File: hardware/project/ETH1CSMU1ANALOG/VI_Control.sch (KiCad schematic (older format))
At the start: 156 parts

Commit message: Base board schematic.
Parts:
- added C? (x2): 2u2, symbol Device:C
- added C? (x2): 100n, symbol Device:C
- added D? (x2): BZT52B15LP, symbol Device:D_Zener
- added R? (x2): 2k2, symbol Device:R
- added R? (x2): 3k57, symbol Device:R
- added U?: ADS8517, symbol ETH1CSMU1:ADS8517
- TP?: value +/- -> POLARITY
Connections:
- net +15VF: now also U?.13 (V+), U?.13 (V+), U?.13 (V+), U?.6 (V+), U?.6 (V+), U?.6 (V+), R?.2
- net -15VF: now also U?.2 (V-), U?.2 (V-), U?.2 (V-), U?.4 (V-), U?.4 (V-), U?.4 (V-), R?.2
- net GNDB: now also C?.2, C?.2
- net GNDP: now also C?.2, C?.2, U?.14 (DGND), U?.2 (AGND1), U?.20 (TAG), U?.25 (PWRD), U?.26 (REFD), U?.6 (AGND2), U?.7 (SB/~BTC)
- net GNDS: now also U?.21 (BYTE)
- net at C?.2, R?.2, U?.6: now also U?.1 (R1IN)
- net +3.3VF renamed +3.3DVF
- net +3.3DVF: now also U?.28 (VDIG), U?.8 (EXT/~IN)
- new net: C?.1, U?.3 (R2IN), U?.4 (CAP)
- new net: C?.1, U?.5 (REF)
- new net +30VF: C?.1, R?.2
- new net +5VF: U?.27 (VANA)
- new net +BOT_DRIVE: D?.2 (A)
- new net +TOP_DRIVE: D?.1 (K), R?.1
- new net +ZENER: R?.1
- new net -30VF: C?.1, R?.2
- new net -BOT_DRIVE: D?.1 (K)
- new net -TOP_DRIVE: D?.2 (A), R?.1
- new net -ZENER: R?.1
- new net ADC_DATACLK: U?.18 (DATACLK)
- new net ADC_R\~C: U?.22 (R/~C)
- new net ADC_SDATA: U?.19 (SDATA)
- new net ADC_~BUSY: U?.24 (~BUSY)
- new net ADC_~CS: U?.23 (~CS)
- no-connect marks 18 -> 26
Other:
- moved on the sheet: TP?

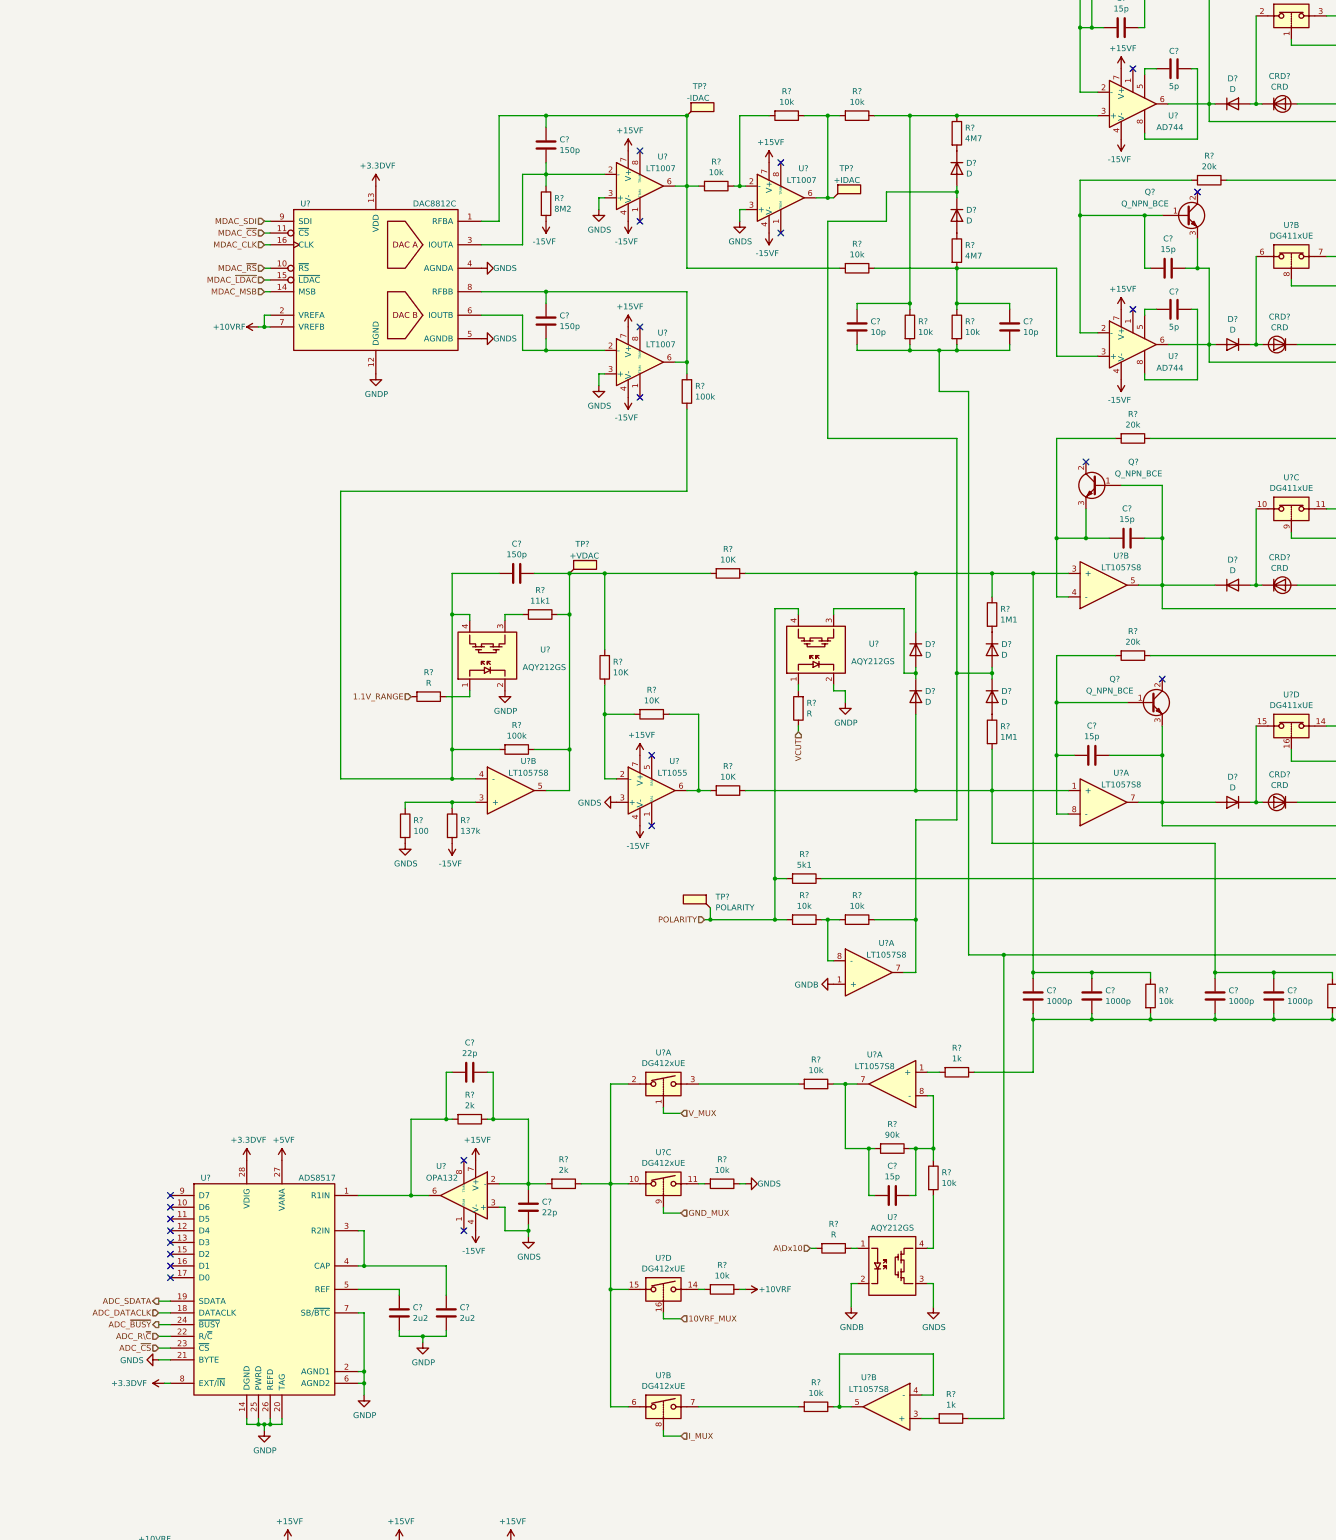
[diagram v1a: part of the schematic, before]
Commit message: Footprint assigment
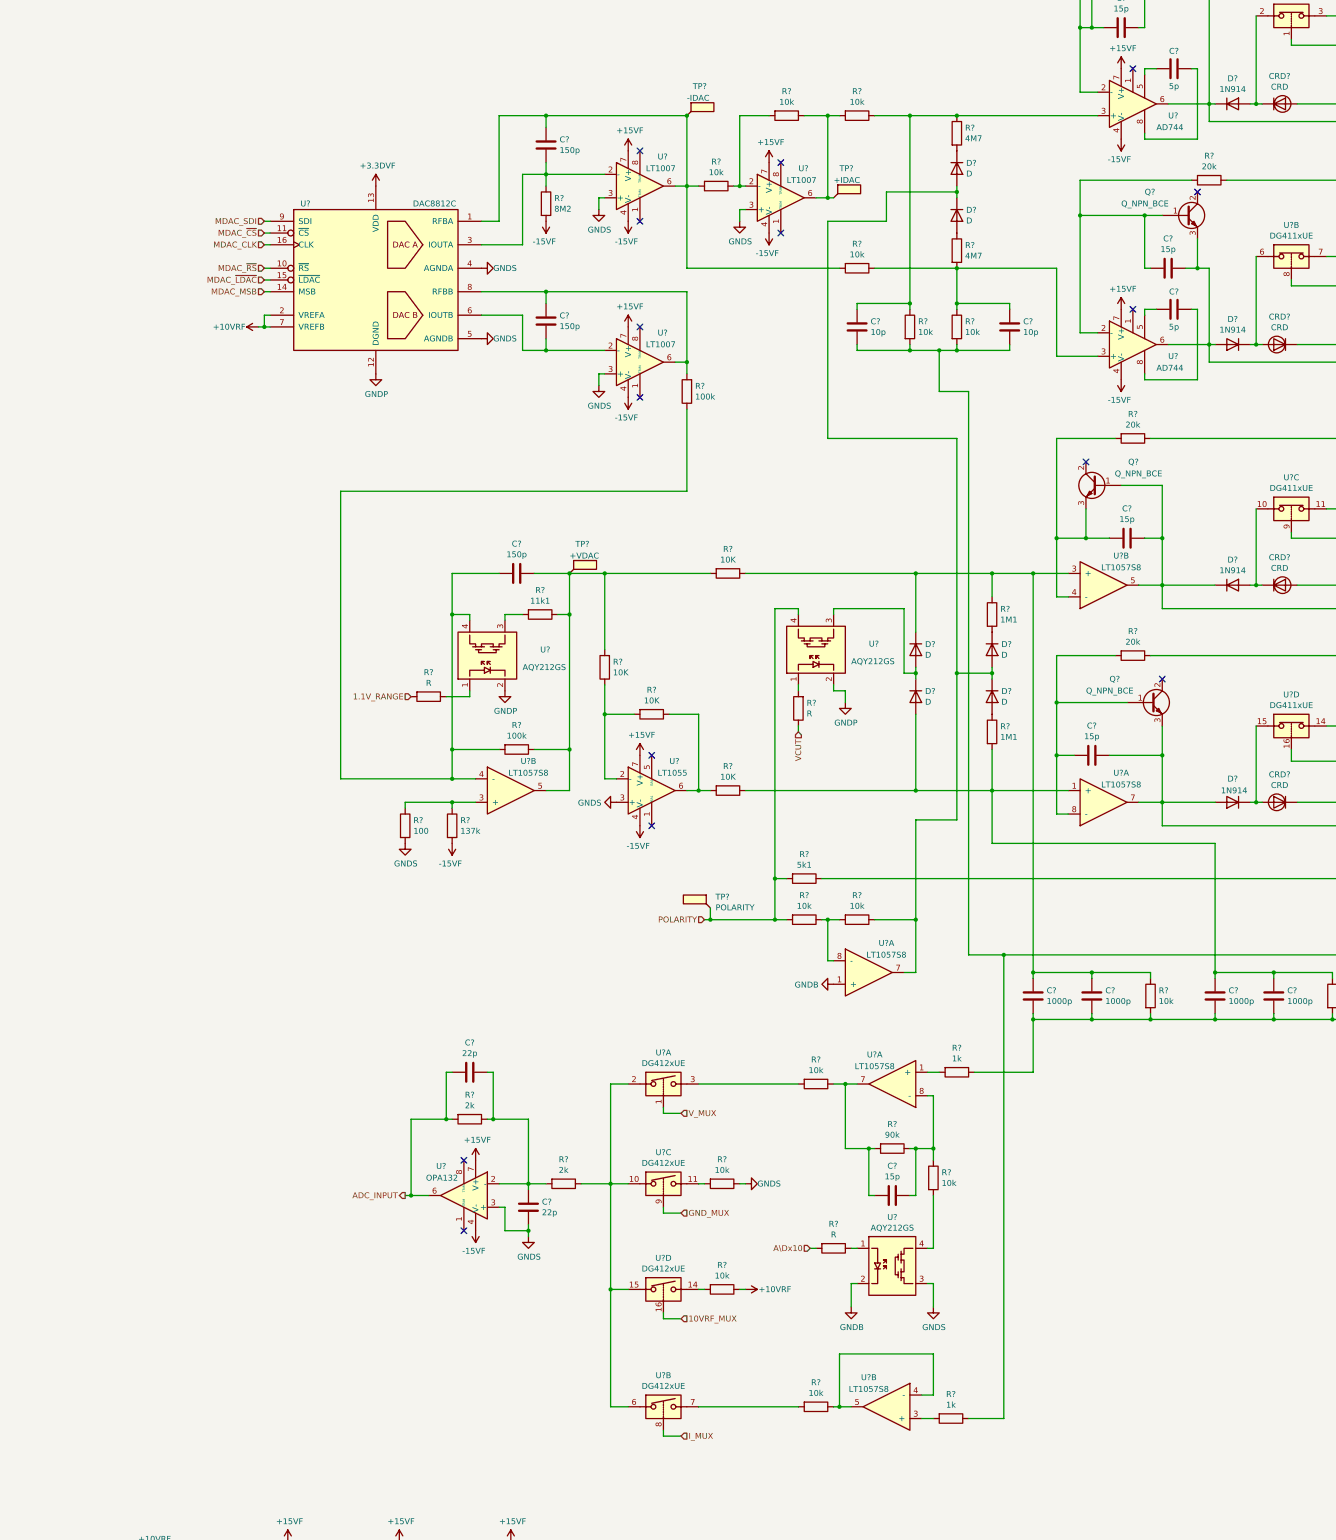
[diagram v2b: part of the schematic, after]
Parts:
- removed C? (x2): 2u2, symbol Device:C
- removed U?: ADS8517, symbol ETH1CSMU1:ADS8517
- D? (x4): value D -> 1N914
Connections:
- net ADC_INPUT: now reaches C?.2, R?.2, U?.6
- no-connect marks 26 -> 18
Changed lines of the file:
@@
 EESchema Schematic File Version 4
-LIBS:ETH1CSMU1ANALOG-cache
 EELAYER 30 0
 EELAYER END
 $Descr A2 23386 16535
 encoding utf-8
-Sheet 2 6
+Sheet 2 7
 Title ""
 Date ""
@@
 P 12800 2250
 F 0 "D?" H 12800 2466 50  0000 C CNN
-F 1 "D" H 12800 2375 50  0000 C CNN
+F 1 "1N914" H 12800 2375 50  0000 C CNN
 F 2 "" H 12800 2250 50  0001 C CNN
 F 3 "~" H 12800 2250 50  0001 C CNN
@@
 P 12800 4300
 F 0 "D?" H 12800 4084 50  0000 C CNN
-F 1 "D" H 12800 4175 50  0000 C CNN
+F 1 "1N914" H 12800 4175 50  0000 C CNN
 F 2 "" H 12800 4300 50  0001 C CNN
 F 3 "~" H 12800 4300 50  0001 C CNN
@@
 P 12800 6350
 F 0 "D?" H 12800 6566 50  0000 C CNN
-F 1 "D" H 12800 6475 50  0000 C CNN
+F 1 "1N914" H 12800 6475 50  0000 C CNN
 F 2 "" H 12800 6350 50  0001 C CNN
 F 3 "~" H 12800 6350 50  0001 C CNN
@@
 U 1 1 5E8136FF
 P 12800 8200
-F 0 "D?" H 12800 7984 50  0000 C CNN
-F 1 "D" H 12800 8075 50  0000 C CNN
+F 0 "D?" H 12800 8000 50  0000 C CNN
+F 1 "1N914" H 12900 8100 50  0000 R CNN
 F 2 "" H 12800 8200 50  0001 C CNN
 F 3 "~" H 12800 8200 50  0001 C CNN
@@
 Wire Wire Line
 	6500 10900 6800 10900
-Connection ~ 5800 11550
 $Comp
 L ETH1CSMU1:+15VF #PWR?
@@
 Connection ~ 8900 9200
 $Comp
-L ETH1CSMU1:ADS8517 U?
-U 1 1 5DDFFCB8
-P 4550 12350
-F 0 "U?" H 4050 13300 50  0000 C CNN
-F 1 "ADS8517" H 5000 13300 50  0000 C CNN
-F 2 "" H 4550 12500 50  0001 C CNN
-F 3 "" H 4550 12500 50  0001 C CNN
-	1    4550 12350
-	1    0    0    -1
-$EndComp
-$Comp
-L ETH1CSMU1:GNDP #PWR?
-U 1 1 5DE1A9F9
-P 4550 13550
-F 0 "#PWR?" H 4550 13300 50  0001 C CNN
-F 1 "GNDP" H 4555 13377 50  0000 C CNN
-F 2 "" H 4550 13550 50  0001 C CNN
-F 3 "" H 4550 13550 50  0001 C CNN
-	1    4550 13550
-	1    0    0    -1
-$EndComp
-Wire Wire Line
-	4400 13450 4400 13500
-Wire Wire Line
-	4400 13500 4500 13500
-Wire Wire Line
-	4700 13500 4700 13450
-Wire Wire Line
-	4600 13450 4600 13500
-Connection ~ 4600 13500
-Wire Wire Line
-	4600 13500 4700 13500
-Wire Wire Line
-	4500 13450 4500 13500
-Connection ~ 4500 13500
-Wire Wire Line
-	4500 13500 4550 13500
-Wire Wire Line
-	4550 13550 4550 13500
-Connection ~ 4550 13500
-Wire Wire Line
-	4550 13500 4600 13500
-Wire Wire Line
-	5350 11550 5800 11550
-NoConn ~ 3750 11550
-NoConn ~ 3750 11650
-NoConn ~ 3750 11750
-NoConn ~ 3750 11850
-NoConn ~ 3750 11950
-NoConn ~ 3750 12050
-NoConn ~ 3750 12150
-NoConn ~ 3750 12250
-Wire Wire Line
-	3750 12450 3650 12450
-Wire Wire Line
-	3750 12550 3650 12550
-Wire Wire Line
-	3750 12650 3650 12650
-Wire Wire Line
-	3750 12750 3650 12750
-Wire Wire Line
-	3750 12850 3650 12850
-$Comp
-L ETH1CSMU1:GNDS #PWR?
-U 1 1 5E53DD24
-P 3650 12950
-F 0 "#PWR?" H 3650 12700 50  0001 C CNN
-F 1 "GNDS" V 3655 12822 50  0000 R CNN
-F 2 "" H 3650 12950 50  0001 C CNN
-F 3 "" H 3650 12950 50  0001 C CNN
-	1    3650 12950
-	0    1    1    0
-$EndComp
-Wire Wire Line
-	3750 13150 3700 13150
-Wire Wire Line
-	5350 12150 5400 12150
-Wire Wire Line
-	5400 12150 5400 11850
-Wire Wire Line
-	5400 11850 5350 11850
-$Comp
-L Device:C C?
-U 1 1 5E6A31E2
-P 5700 12550
-F 0 "C?" H 5815 12596 50  0000 L CNN
-F 1 "2u2" H 5815 12505 50  0000 L CNN
-F 2 "" H 5738 12400 50  0001 C CNN
-F 3 "~" H 5700 12550 50  0001 C CNN
-	1    5700 12550
-	1    0    0    -1
-$EndComp
-$Comp
-L Device:C C?
-U 1 1 5E6A4FBB
-P 6100 12550
-F 0 "C?" H 6215 12596 50  0000 L CNN
-F 1 "2u2" H 6215 12505 50  0000 L CNN
-F 2 "" H 6138 12400 50  0001 C CNN
-F 3 "~" H 6100 12550 50  0001 C CNN
-	1    6100 12550
-	1    0    0    -1
-$EndComp
-Wire Wire Line
-	5700 12400 5700 12350
-Wire Wire Line
-	5700 12350 5350 12350
-Wire Wire Line
-	5400 12150 6100 12150
-Wire Wire Line
-	6100 12150 6100 12400
-Connection ~ 5400 12150
-Wire Wire Line
-	5700 12700 5700 12750
-Wire Wire Line
-	5700 12750 5900 12750
-Wire Wire Line
-	6100 12750 6100 12700
-$Comp
-L ETH1CSMU1:GNDP #PWR?
-U 1 1 5E7BD417
-P 5900 12800
-F 0 "#PWR?" H 5900 12550 50  0001 C CNN
-F 1 "GNDP" H 5905 12627 50  0000 C CNN
-F 2 "" H 5900 12800 50  0001 C CNN
-F 3 "" H 5900 12800 50  0001 C CNN
-	1    5900 12800
-	1    0    0    -1
-$EndComp
-Wire Wire Line
-	5900 12800 5900 12750
-Connection ~ 5900 12750
-Wire Wire Line
-	5900 12750 6100 12750
-Wire Wire Line
-	5350 12550 5400 12550
-Wire Wire Line
-	5400 12550 5400 13050
-Wire Wire Line
-	5400 13150 5350 13150
-Wire Wire Line
-	5350 13050 5400 13050
-Connection ~ 5400 13050
-Wire Wire Line
-	5400 13050 5400 13150
-$Comp
-L ETH1CSMU1:GNDP #PWR?
-U 1 1 5E937FD2
-P 5400 13250
-F 0 "#PWR?" H 5400 13000 50  0001 C CNN
-F 1 "GNDP" H 5405 13077 50  0000 C CNN
-F 2 "" H 5400 13250 50  0001 C CNN
-F 3 "" H 5400 13250 50  0001 C CNN
-	1    5400 13250
-	1    0    0    -1
-$EndComp
-Wire Wire Line
-	5400 13250 5400 13150
-Connection ~ 5400 13150
-Wire Wire Line
-	3650 12950 3750 12950
-$Comp
-L ETH1CSMU1:+3.3DVF #PWR?
-U 1 1 5EA03ABD
-P 3700 13150
-F 0 "#PWR?" H 3700 13000 50  0001 C CNN
-F 1 "+3.3DVF" V 3700 13300 50  0000 L CNN
-F 2 "" H 3700 13150 50  0001 C CNN
-F 3 "" H 3700 13150 50  0001 C CNN
-	1    3700 13150
-	0    -1   -1   0
-$EndComp
-$Comp
 L ETH1CSMU1:+3.3DVF #PWR?
 U 1 1 5EA113CF
@@
 $EndComp
 $Comp
-L ETH1CSMU1:+3.3DVF #PWR?
-U 1 1 5EA1DD31
-P 4400 11250
-F 0 "#PWR?" H 4400 11100 50  0001 C CNN
-F 1 "+3.3DVF" H 4415 11423 50  0000 C CNN
-F 2 "" H 4400 11250 50  0001 C CNN
-F 3 "" H 4400 11250 50  0001 C CNN
-	1    4400 11250
-	1    0    0    -1
-$EndComp
-$Comp
-L ETH1CSMU1:+5VF #PWR?
-U 1 1 5EA1F025
-P 4700 11250
-F 0 "#PWR?" H 4700 11100 50  0001 C CNN
-F 1 "+5VF" H 4715 11423 50  0000 C CNN
-F 2 "" H 4700 11250 50  0001 C CNN
-F 3 "" H 4700 11250 50  0001 C CNN
-	1    4700 11250
-	1    0    0    -1
-$EndComp
-Text HLabel 3650 12450 0    50   Output ~ 0
-ADC_SDATA
-Text HLabel 3650 12550 0    50   Input ~ 0
-ADC_DATACLK
-Text HLabel 3650 12650 0    50   Output ~ 0
-ADC_~BUSY
-Text HLabel 3650 12750 0    50   Input ~ 0
-ADC_R\~C
-Text HLabel 3650 12850 0    50   Input ~ 0
-ADC_~CS
-$Comp
 L ETH1CSMU1:+15VF #PWR?
 U 1 1 5EAEF03C
@@
 	1    0    0    -1
 $EndComp
+Text HLabel 5750 11550 0    50   Output ~ 0
+ADC_INPUT
+Wire Wire Line
+	5750 11550 5800 11550
+Connection ~ 5800 11550
 $EndSCHEMATC
